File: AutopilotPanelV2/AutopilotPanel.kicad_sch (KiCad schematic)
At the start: 144 parts, among them J1 USB_C_Receptacle_USB2.0_16P, J2 PINHD_1x2_Male, J3 PINHD_1x2_Male, J4 PINHD_1x2_Male, J5 PINHD_1x2_Male, J6 PINHD_1x2_Male, J7 PINHD_1x2_Male, Q1 NFET-SOT23, Q2 NFET-SOT23, Q3 NFET-SOT23, Q4 NFET-SOT23, Q5 NFET-SOT23, Q6 NFET-SOT23, SW1 SW_SPST_Tactile_6x6, SW10 SW_SPST_Tactile_6x6, SW11 SW_SPST_Tactile_6x6, SW12 SW_SPST_Tactile_6x6, SW13 SW_SPST_Tactile_6x6, SW14 SW_SPST_Tactile_6x6, SW15 RotaryEncoder_Switch_EC11E, SW2 SW_SPST_Tactile_6x6, SW3 SW_SPST_Tactile_6x6, SW4 SW_SPST_Tactile_6x6, SW5 SW_SPST_Tactile_6x6, SW6 SW_SPST_Tactile_6x6, SW7 SW_SPST_Tactile_6x6, SW8 SW_SPST_Tactile_6x6, SW9 SW_SPST_Tactile_6x6, U1 74HC164, U10 7SegmentFJ5161AH, U11 7SegmentFJ5161AH, U12 7SegmentFJ5161AH, U13 7SegmentFJ5161AH, U14 7SegmentFJ5161AH, U15 74HC165, U16 TPS62160DSG, U17 74HC165, U2 74HC164, U3 74HC164, U4 74HC164, U5 74HC164, U6 74HC164, U7 74HC164, U8 74HC164, U9 7SegmentFJ5161AH

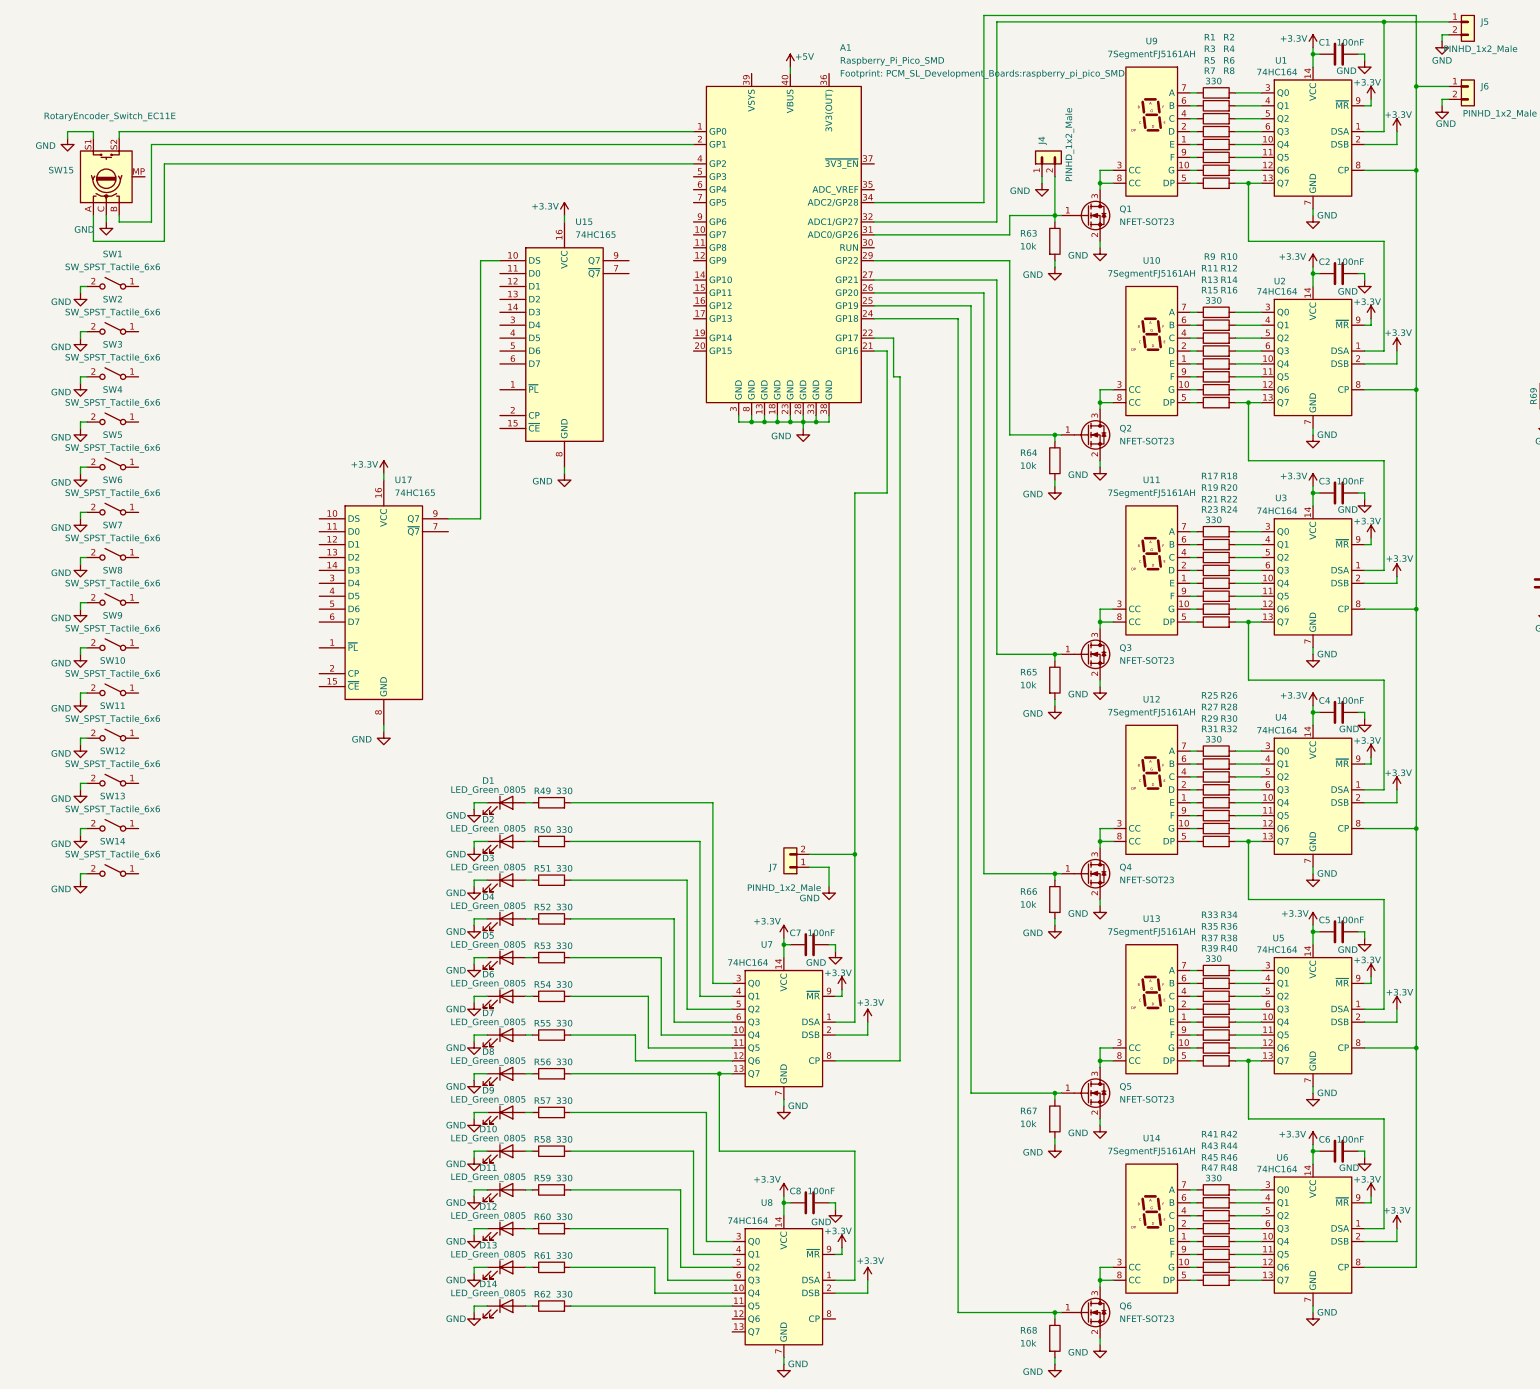
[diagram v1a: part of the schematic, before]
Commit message: 7Segment shift registers changed from 74HC164 to 74HC595
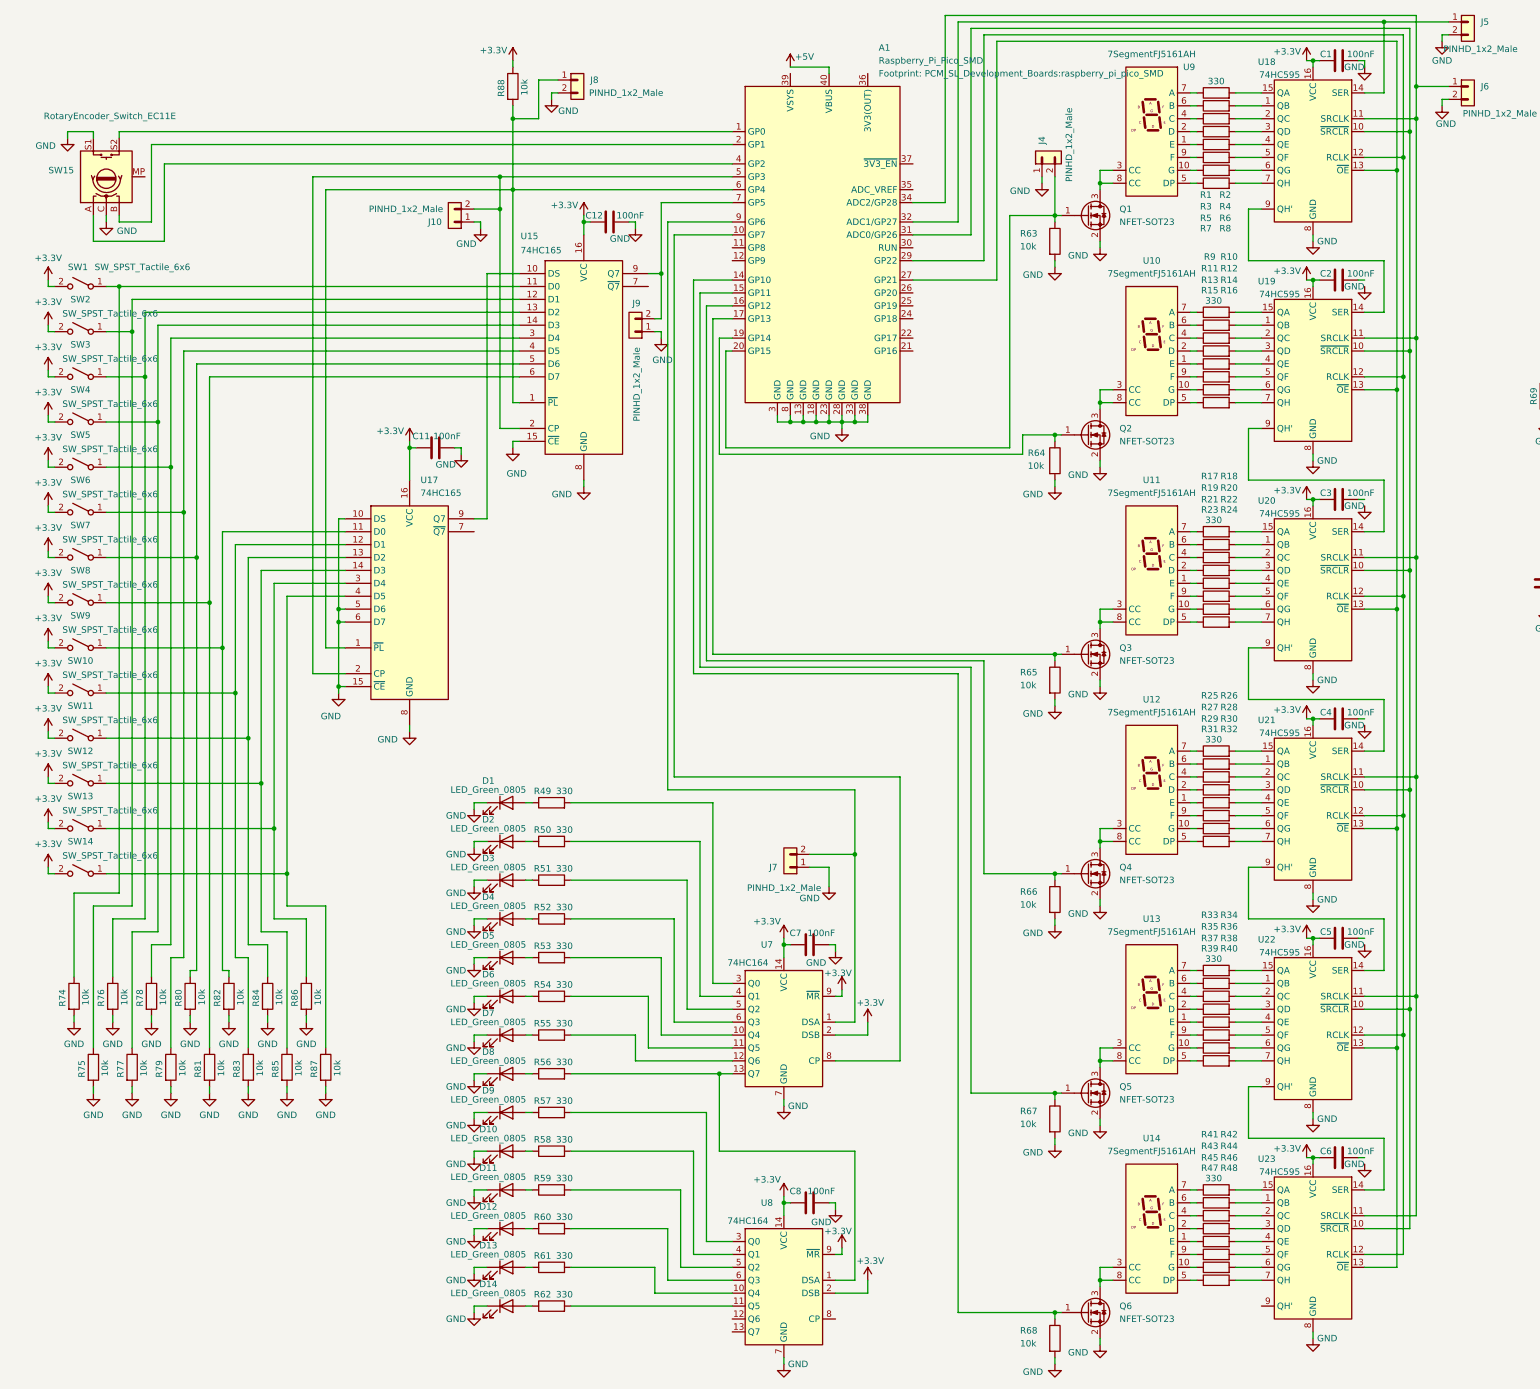
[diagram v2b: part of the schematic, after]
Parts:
- removed U1, U2, U3, U4, U5, U6: 74HC164, Package_SO:SOIC-14_3.9x8.7mm_P1.27mm, symbol 74xx:74HC164
- added C11, C12: 100nF, Capacitor_SMD:C_0603_1608Metric, symbol Device:C
- added J10, J8, J9: PINHD_1x2_Male, Connector_PinHeader_2.54mm:PinHeader_1x02_P2.54mm_Vertical, symbol PCM_SL_Pin_Headers:PINHD_1x2_Male
- added R74, R75, R76, R77, R78, R79, R80, R81, R82, R83, R84, R85, R86, R87, R88: 10k, Resistor_SMD:R_0603_1608Metric, symbol Device:R
- added U18, U19, U20, U21, U22, U23: 74HC595, symbol 74xx:74HC595
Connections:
- net +3.3V: now also SW1.2 (B), SW10.2 (B), SW11.2 (B), SW12.2 (B), SW13.2 (B), SW14.2 (B), SW2.2 (B), SW3.2 (B), SW4.2 (B), SW5.2 (B), SW6.2 (B), SW7.2 (B), SW8.2 (B), SW9.2 (B), C11.1, C12.1, R88.1, U18.16 (VCC), U19.16 (VCC), U20.16 (VCC), U21.16 (VCC), U22.16 (VCC), U23.16 (VCC)
- net GND: now also U15.15 (~{CE}), U17.10 (DS), U17.15 (~{CE}), U17.5 (D6), U17.6 (D7), C11.2, C12.2, J10.1, J8.2, J9.1, R74.2, R75.2, R76.2, R77.2, R78.2, R79.2, R80.2, R81.2, R82.2, R83.2, R84.2, R85.2, R86.2, R87.2, U18.8 (GND), U19.8 (GND), U20.8 (GND), U21.8 (GND), U22.8 (GND), U23.8 (GND); no longer C2.2, C3.2, C4.2, C5.2, C6.2, SW1.2 (B), SW10.2 (B), SW11.2 (B), SW12.2 (B), SW13.2 (B), SW14.2 (B), SW2.2 (B), SW3.2 (B), SW4.2 (B), SW5.2 (B), SW6.2 (B), SW7.2 (B), SW8.2 (B), SW9.2 (B)
- net at SW1.1 (A): now also U15.11 (D0), R74.1
- net at Q3.1 (G), R65.1: now also A1.17 (GP13); no longer A1.27 (GP21)
- net at Q2.1 (G), R64.1: now also A1.19 (GP14); no longer A1.29 (GP22)
- net at SW11.1 (A): now also U17.13 (D2), R84.1
- net at Q5.1 (G), R67.1: now also A1.15 (GP11); no longer A1.25 (GP19)
- net at R11.2: now also U19.2 (QC)
- net at R6.2: now also U18.5 (QF)
- net at SW7.1 (A): now also U15.5 (D6), R80.1
- net at R14.2: now also U19.5 (QF)
- net at R1.2: now also U18.15 (QA)
- net at Q4.1 (G), R66.1: now also A1.16 (GP12); no longer A1.26 (GP20)
- net at R33.2: now also U22.15 (QA)
- net at R12.2: now also U19.3 (QD)
- net at R43.2: now also U23.2 (QC)
- net at R46.2: now also U23.5 (QF)
- net at R16.2: now also U19.7 (QH)
- net at SW12.1 (A): now also U17.14 (D3), R85.1
- net at R23.2: now also U20.6 (QG)
- net at R4.2: now also U18.3 (QD)
- net at R39.2: now also U22.6 (QG)
- net at SW2.1 (A): now also U15.12 (D1), R75.1
- net at SW9.1 (A): now also U17.11 (D0), R82.1
- net at R13.2: now also U19.4 (QE)
- net at R19.2: now also U20.2 (QC)
- net at R20.2: now also U20.3 (QD)
- net at SW8.1 (A): now also U15.6 (D7), R81.1
- net at R32.2: now also U21.7 (QH)
- net at R37.2: now also U22.4 (QE)
- net at R38.2: now also U22.5 (QF)
- net at R40.2: now also U22.7 (QH)
- net at R34.2: now also U22.1 (QB)
- net at R35.2: now also U22.2 (QC)
- net at R36.2: now also U22.3 (QD)
- net at A1.34 (ADC2/GP28), J6.1: now also U18.11 (SRCLK), U19.11 (SRCLK), U20.11 (SRCLK), U21.11 (SRCLK), U22.11 (SRCLK), U23.11 (SRCLK)
- net at R45.2: now also U23.4 (QE)
- net at R9.2: now also U19.15 (QA)
- net at R27.2: now also U21.2 (QC)
- net at R28.2: now also U21.3 (QD)
- net at R8.2: now also U18.7 (QH)
- net at R15.2: now also U19.6 (QG)
- net at R10.2: now also U19.1 (QB)
- net at R3.2: now also U18.2 (QC)
- net at A1.32 (ADC1/GP27), J5.1: now also U18.14 (SER)
- net at R5.2: now also U18.4 (QE)
- net at R7.2: now also U18.6 (QG)
- net at R2.2: now also U18.1 (QB)
- net at R29.2: now also U21.4 (QE)
- net at R25.2: now also U21.15 (QA)
- net at Q6.1 (G), R68.1: now also A1.14 (GP10); no longer A1.24 (GP18)
- net at R17.2: now also U20.15 (QA)
- net at R47.2: now also U23.6 (QG)
- net at R41.2: now also U23.15 (QA)
- net at R24.2: now also U20.7 (QH)
- net at R30.2: now also U21.5 (QF)
- net at R31.2: now also U21.6 (QG)
- net at R26.2: now also U21.1 (QB)
- net at SW10.1 (A): now also U17.12 (D1), R83.1
- net at R42.2: now also U23.1 (QB)
- net at R48.2: now also U23.7 (QH)
- net at SW13.1 (A): now also U17.3 (D4), R86.1
- net at A1.10 (GP7): now also U7.8 (CP)
- net at A1.20 (GP15): now also J4.2, Q1.1 (G), R63.1
- net at J7.2, U7.1 (DSA): now also A1.9 (GP6); no longer A1.21 (GP16)
- net at A1.22 (GP17): no longer U7.8 (CP)
- net at A1.5 (GP3): now also U15.2 (CP), U17.2 (CP), J10.2
- net at A1.6 (GP4): now also U15.1 (~{PL}), U17.1 (~{PL}), J8.1, R88.2
- net at A1.7 (GP5): now also U15.9 (Q7), J9.2
- net at R44.2: now also U23.3 (QD)
- net at U17.4 (D5): now also SW14.1 (A), R87.1
- net at SW5.1 (A): now also U15.3 (D4), R78.1
- net at R22.2: now also U20.5 (QF)
- net at R18.2: now also U20.1 (QB)
- net at R21.2: now also U20.4 (QE)
- net at U15.13 (D2): now also SW3.1 (A), R76.1
- net at U15.14 (D3): now also SW4.1 (A), R77.1
- net at U15.4 (D5): now also SW6.1 (A), R79.1
- new net: A1.31 (ADC0/GP26), U18.10 (~{SRCLR}), U19.10 (~{SRCLR}), U20.10 (~{SRCLR}), U21.10 (~{SRCLR}), U22.10 (~{SRCLR}), U23.10 (~{SRCLR})
- new net: A1.29 (GP22), U18.12 (RCLK), U19.12 (RCLK), U20.12 (RCLK), U21.12 (RCLK), U22.12 (RCLK), U23.12 (RCLK)
- new net: A1.27 (GP21), U18.13 (~{OE}), U19.13 (~{OE}), U20.13 (~{OE}), U21.13 (~{OE}), U22.13 (~{OE}), U23.13 (~{OE})
- new net: U22.9 (QH'), U23.14 (SER)
- new net: U21.9 (QH'), U22.14 (SER)
- new net: U18.9 (QH'), U19.14 (SER)
- new net: U20.9 (QH'), U21.14 (SER)
- new net: U19.9 (QH'), U20.14 (SER)
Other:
- moved on the sheet: A1, C1, SW1, U15, U17
